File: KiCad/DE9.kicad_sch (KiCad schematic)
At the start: 1 part, among them J2 DE9_Socket

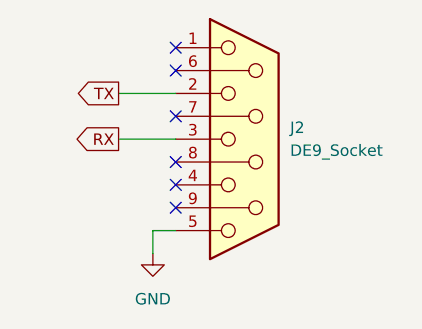
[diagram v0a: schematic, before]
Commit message: ArregLATS ERRORS ERC
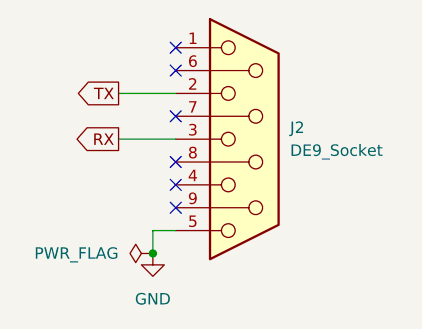
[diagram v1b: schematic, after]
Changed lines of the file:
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@@
 	(generator_version "9.0")
 	(paper "A4")
+	(junction
+		(at 119.38 104.14)
+		(diameter 0)
+		(color 0 0 0 0)
+	)
 	(no_connect
 		(at 121.92 88.9)
@@
 				(justify right)
 				(hide yes)
+			)
+		)
+	)
+	(symbol
+		(lib_id "power:PWR_FLAG")
+		(at 119.38 104.14 90)
+		(unit 1)
+		(exclude_from_sim no)
+		(in_bom yes)
+		(on_board yes)
+		(dnp no)
+		(fields_autoplaced yes)
+		(property "Reference" "#FLG?"
+			(at 117.475 104.14 0)
+			(effects
+				(font
+					(size 1.27 1.27)
+				)
+				(hide yes)
+			)
+		)
+		(property "Value" "PWR_FLAG"
+			(at 115.57 104.1399 90)
+			(effects
+				(font
+					(size 1.27 1.27)
+				)
+				(justify left)
+			)
+		)
+		(property "Footprint" ""
+			(at 119.38 104.14 0)
+			(effects
+				(font
+					(size 1.27 1.27)
+				)
+				(hide yes)
+			)
+		)
+		(property "Datasheet" "~"
+			(at 119.38 104.14 0)
+			(effects
+				(font
+					(size 1.27 1.27)
+				)
+				(hide yes)
+			)
+		)
+		(property "Description" "Special symbol for telling ERC where power comes from"
+			(at 119.38 104.14 0)
+			(effects
+				(font
+					(size 1.27 1.27)
+				)
+				(hide yes)
+			)
+		)
+		(pin "1"
+		)
+		(instances
+			(project "SEIENTS_EDD"
+				(path "/b6401b4f-5426-49b8-bb2e-8ecdb19989ef/3142985d-1a80-479c-952b-7787fc571509"
+					(reference "#FLG?")
+					(unit 1)
+				)
+			)
+			(project ""
+				(path "/d6ac17ed-b98e-42c6-9547-d03acde0238c"
+					(reference "#FLG01")
+					(unit 1)
+				)
 			)
 		)
@@
 				)
 			)
+			(project "DE9"
+				(path "/d6ac17ed-b98e-42c6-9547-d03acde0238c"
+					(reference "J4")
+					(unit 1)
+				)
+			)
 		)
 	)
@@
 				)
 			)
-		)
-	)
+			(project "DE9"
+				(path "/d6ac17ed-b98e-42c6-9547-d03acde0238c"
+					(reference "#PWR0101")
+					(unit 1)
+				)
+			)
+		)
+	)
+	(sheet_instances
+		(path "/"
+			(page "1")
+		)
+	)
+	(embedded_fonts no)
 )

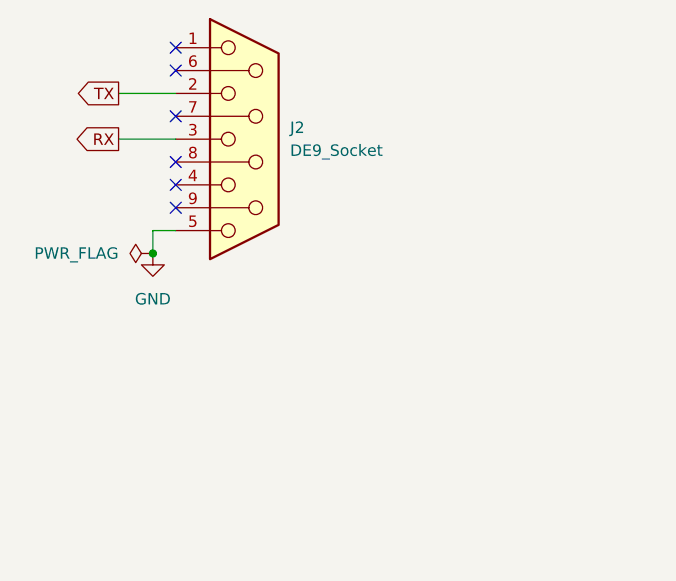
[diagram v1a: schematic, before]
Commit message: Modificacions al DE-9
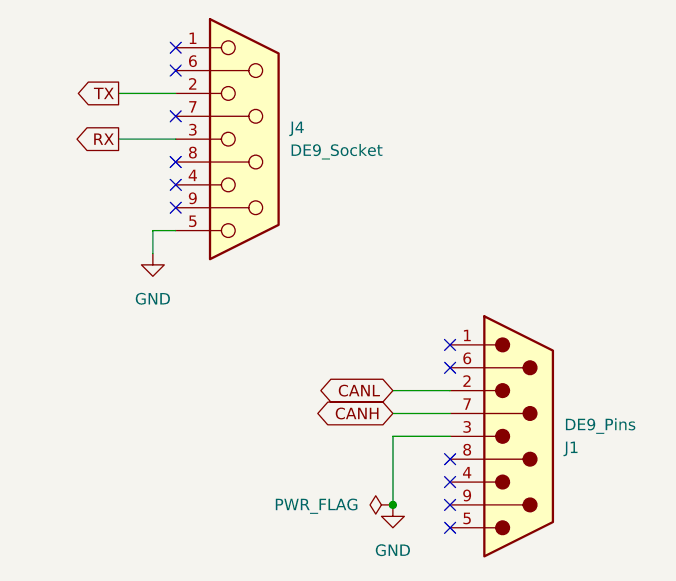
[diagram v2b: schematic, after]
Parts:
- added J1: DE9_Pins, symbol Connector:DE9_Pins
- renumbered J2 to J4
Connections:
- net GND: now also J1.3
- new net CANH: J1.7
- new net CANL: J1.2
- no-connect marks 6 -> 12

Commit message: Modificacions Micro
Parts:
- renumbered J4 to J2, J1 to J6
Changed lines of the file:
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@@
 	(generator_version "9.0")
 	(paper "A4")
-	(junction
-		(at 146.05 132.08)
-		(diameter 0)
-		(color 0 0 0 0)
-	)
 	(no_connect
 		(at 121.92 88.9)
@@
 		(dnp no)
 		(fields_autoplaced yes)
-		(property "Reference" "J4"
+		(property "Reference" "J2"
 			(at 134.62 90.1699 0)
 			(effects
@@
 				(path "/d6ac17ed-b98e-42c6-9547-d03acde0238c"
 					(reference "J4")
-					(unit 1)
-				)
-			)
-		)
-	)
-	(symbol
-		(lib_id "power:PWR_FLAG")
-		(at 146.05 132.08 90)
-		(unit 1)
-		(exclude_from_sim no)
-		(in_bom yes)
-		(on_board yes)
-		(dnp no)
-		(fields_autoplaced yes)
-		(property "Reference" "#FLG02"
-			(at 144.145 132.08 0)
-			(effects
-				(font
-					(size 1.27 1.27)
-				)
-				(hide yes)
-			)
-		)
-		(property "Value" "PWR_FLAG"
-			(at 142.24 132.0799 90)
-			(effects
-				(font
-					(size 1.27 1.27)
-				)
-				(justify left)
-			)
-		)
-		(property "Footprint" ""
-			(at 146.05 132.08 0)
-			(effects
-				(font
-					(size 1.27 1.27)
-				)
-				(hide yes)
-			)
-		)
-		(property "Datasheet" "~"
-			(at 146.05 132.08 0)
-			(effects
-				(font
-					(size 1.27 1.27)
-				)
-				(hide yes)
-			)
-		)
-		(property "Description" "Special symbol for telling ERC where power comes from"
-			(at 146.05 132.08 0)
-			(effects
-				(font
-					(size 1.27 1.27)
-				)
-				(hide yes)
-			)
-		)
-		(pin "1"
-		)
-		(instances
-			(project "DE9"
-				(path "/d6ac17ed-b98e-42c6-9547-d03acde0238c"
-					(reference "#FLG02")
 					(unit 1)
 				)
@@
 		(dnp no)
 		(fields_autoplaced yes)
-		(property "Reference" "#PWR0101"
+		(property "Reference" "#PWR010"
 			(at 119.38 110.49 0)
 			(effects
@@
 		(on_board yes)
 		(dnp no)
-		(property "Reference" "J1"
+		(property "Reference" "J6"
 			(at 165.1 125.7301 0)
 			(effects
@@
 		)
 		(instances
+			(project "SEIENTS_EDD"
+				(path "/b6401b4f-5426-49b8-bb2e-8ecdb19989ef/3142985d-1a80-479c-952b-7787fc571509"
+					(reference "J6")
+					(unit 1)
+				)
+			)
 			(project ""
 				(path "/d6ac17ed-b98e-42c6-9547-d03acde0238c"
@@
 		(dnp no)
 		(fields_autoplaced yes)
-		(property "Reference" "#PWR01"
+		(property "Reference" "#PWR047"
 			(at 146.05 138.43 0)
 			(effects
@@
 		)
 		(instances
+			(project "SEIENTS_EDD"
+				(path "/b6401b4f-5426-49b8-bb2e-8ecdb19989ef/3142985d-1a80-479c-952b-7787fc571509"
+					(reference "#PWR047")
+					(unit 1)
+				)
+			)
 			(project "DE9"
 				(path "/d6ac17ed-b98e-42c6-9547-d03acde0238c"

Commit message: Començat el LAYOUT
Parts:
- J2: footprint (none) -> Connector_Dsub:DSUB-9_Socket_Horizontal_P2.77x2.84mm_EdgePinOffset4.94mm_Housed_MountingHolesOffset4.94mm
- J6: footprint (none) -> Connector_Dsub:DSUB-9_Pins_Horizontal_P2.77x2.84mm_EdgePinOffset4.94mm_Housed_MountingHolesOffset4.94mm
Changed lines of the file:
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@@
 			)
 		)
-		(property "Footprint" ""
+		(property "Footprint" "Connector_Dsub:DSUB-9_Socket_Horizontal_P2.77x2.84mm_EdgePinOffset4.94mm_Housed_MountingHolesOffset4.94mm"
 			(at 129.54 91.44 0)
 			(effects
@@
 			)
 		)
-		(property "Footprint" ""
+		(property "Footprint" "Connector_Dsub:DSUB-9_Pins_Horizontal_P2.77x2.84mm_EdgePinOffset4.94mm_Housed_MountingHolesOffset4.94mm"
 			(at 160.02 124.46 0)
 			(effects
